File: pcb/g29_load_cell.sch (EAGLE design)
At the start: 6 parts, among them IC1 INA122P

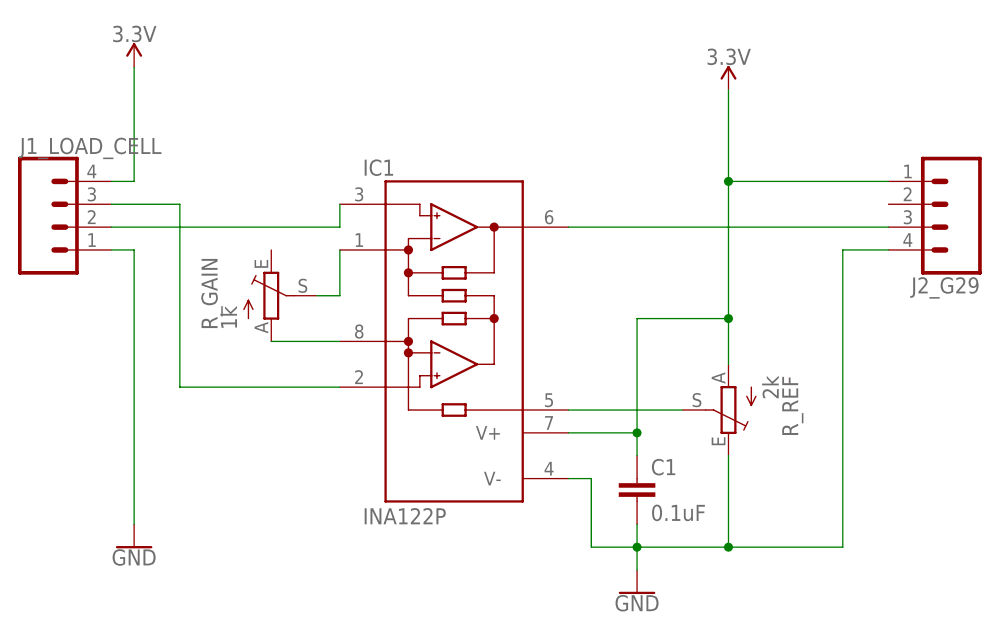
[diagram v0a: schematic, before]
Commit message: fixed ERC errors
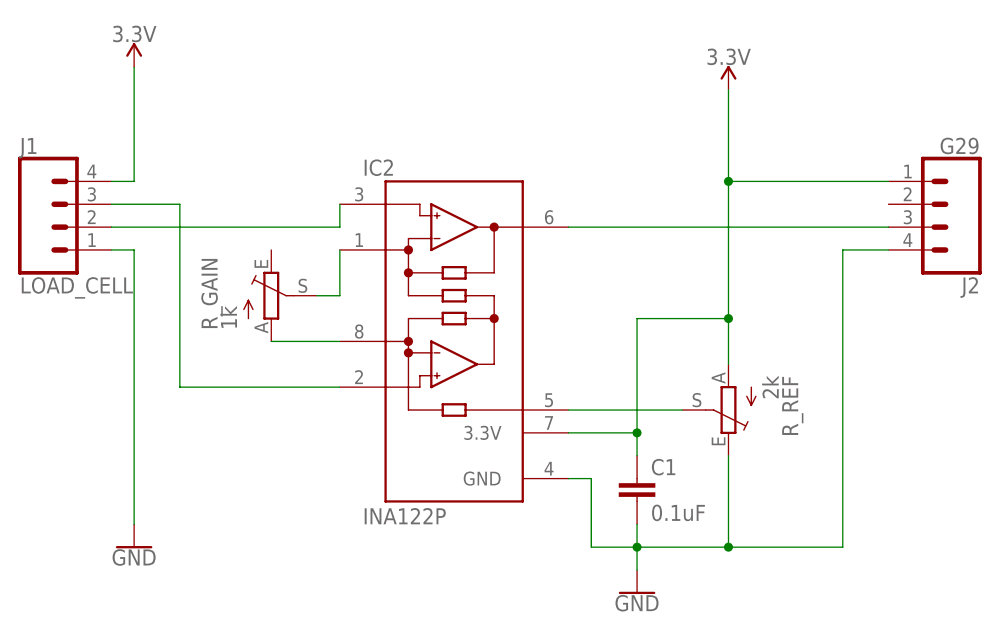
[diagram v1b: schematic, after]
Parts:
- removed IC1: INA122P, burr-brown:INA122P
- added IC2: INA122P, g29_load_cell:INA122P
- J1: value (none) -> LOAD_CELL
- J2: value (none) -> G29
- renumbered J1_LOAD_CELL to J1, J2_G29 to J2
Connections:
- net 3.3V: now also IC2.3.3V; no longer IC1.V+
- net GND: now also IC2.GND; no longer IC1.V-
- net N$1: now also IC2.RG@1; no longer IC1.RG@1
- net N$2: now also IC2.RG; no longer IC1.RG
- net N$3: now also IC2.+IN; no longer IC1.+IN
- net N$4: now also IC2.-IN; no longer IC1.-IN
- net N$6: now also IC2.REF; no longer IC1.REF
- net N$7: now also IC2.OUT; no longer IC1.OUT
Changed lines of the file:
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@@
 </classes>
 <parts>
-<part name="IC1" library="burr-brown" library_urn="urn:adsk.eagle:library:111" deviceset="INA122" device="P" package3d_urn="urn:adsk.eagle:package:4906/1"/>
 <part name="C1" library="rcl" library_urn="urn:adsk.eagle:library:334" deviceset="C-EU" device="025-024X044" package3d_urn="urn:adsk.eagle:package:23630/1" value="0.1uF"/>
 <part name="R_GAIN" library="pot" library_urn="urn:adsk.eagle:library:331" deviceset="TRIM_EU-" device="RJ9W" package3d_urn="urn:adsk.eagle:package:22702/1" value="1k"/>
 <part name="R_REF" library="pot" library_urn="urn:adsk.eagle:library:331" deviceset="TRIM_EU-" device="RJ9W" package3d_urn="urn:adsk.eagle:package:22702/1" value="2k"/>
-<part name="J1_LOAD_CELL" library="SparkFun-Connectors" deviceset="CONN_04" device="SCREW"/>
-<part name="J2_G29" library="SparkFun-Connectors" deviceset="CONN_04" device="SCREW"/>
+<part name="J1" library="SparkFun-Connectors" deviceset="CONN_04" device="SCREW" value="LOAD_CELL"/>
+<part name="J2" library="SparkFun-Connectors" deviceset="CONN_04" device="SCREW" value="G29"/>
 <part name="SUPPLY1" library="SparkFun-PowerSymbols" deviceset="3.3V" device=""/>
 <part name="GND1" library="SparkFun-PowerSymbols" deviceset="GND" device=""/>
 <part name="GND2" library="SparkFun-PowerSymbols" deviceset="GND" device=""/>
 <part name="SUPPLY2" library="SparkFun-PowerSymbols" deviceset="3.3V" device=""/>
+<part name="IC2" library="g29_load_cell" deviceset="INA122" device="P" package3d_urn="urn:adsk.eagle:package:4906/1"/>
 </parts>
 <sheets>
@@
 </plain>
 <instances>
-<instance part="IC1" gate="G$1" x="20.32" y="2.54" smashed="yes">
-<attribute name="NAME" x="10.16" y="20.955" size="1.778" layer="95" ratio="10"/>
-<attribute name="VALUE" x="10.16" y="-17.78" size="1.778" layer="96" ratio="10"/>
-</instance>
 <instance part="C1" gate="G$1" x="40.64" y="-12.7" smashed="yes">
 <attribute name="NAME" x="42.164" y="-12.319" size="1.778" layer="95"/>
@@
 <attribute name="VALUE" x="54.61" y="-1.27" size="1.778" layer="96" rot="R270"/>
 </instance>
-<instance part="J1_LOAD_CELL" gate="J1" x="-22.86" y="15.24" smashed="yes">
+<instance part="J1" gate="J1" x="-22.86" y="15.24" smashed="yes">
 <attribute name="VALUE" x="-27.94" y="7.874" size="1.778" layer="96" font="vector"/>
 <attribute name="NAME" x="-27.94" y="23.368" size="1.778" layer="95" font="vector"/>
 </instance>
-<instance part="J2_G29" gate="J1" x="73.66" y="17.78" smashed="yes" rot="R180">
+<instance part="J2" gate="J1" x="73.66" y="17.78" smashed="yes" rot="R180">
 <attribute name="VALUE" x="78.74" y="25.146" size="1.778" layer="96" font="vector" rot="R180"/>
 <attribute name="NAME" x="78.74" y="9.652" size="1.778" layer="95" font="vector" rot="R180"/>
@@
 <attribute name="VALUE" x="50.8" y="33.274" size="1.778" layer="96" align="bottom-center"/>
 </instance>
+<instance part="IC2" gate="G$1" x="20.32" y="2.54" smashed="yes">
+<attribute name="NAME" x="10.16" y="20.955" size="1.778" layer="95" ratio="10"/>
+<attribute name="VALUE" x="10.16" y="-17.78" size="1.778" layer="96" ratio="10"/>
+</instance>
 </instances>
 <busses>
@@
 <net name="N$1" class="0">
 <segment>
-<pinref part="IC1" gate="G$1" pin="RG@1"/>
 <pinref part="R_GAIN" gate="1" pin="A"/>
 <wire x1="7.62" y1="2.54" x2="0" y2="2.54" width="0.1524" layer="91"/>
+<pinref part="IC2" gate="G$1" pin="RG@1"/>
 </segment>
 </net>
 <net name="N$2" class="0">
 <segment>
-<pinref part="IC1" gate="G$1" pin="RG"/>
 <pinref part="R_GAIN" gate="1" pin="S"/>
 <wire x1="7.62" y1="12.7" x2="7.62" y2="7.62" width="0.1524" layer="91"/>
 <wire x1="7.62" y1="7.62" x2="5.08" y2="7.62" width="0.1524" layer="91"/>
+<pinref part="IC2" gate="G$1" pin="RG"/>
 </segment>
 </net>
 <net name="GND" class="0">
 <segment>
-<pinref part="J1_LOAD_CELL" gate="J1" pin="1"/>
+<pinref part="J1" gate="J1" pin="1"/>
 <wire x1="-17.78" y1="12.7" x2="-15.24" y2="12.7" width="0.1524" layer="91"/>
 <pinref part="GND1" gate="1" pin="GND"/>
@@
 </segment>
 <segment>
-<pinref part="IC1" gate="G$1" pin="V-"/>
 <wire x1="33.02" y1="-12.7" x2="35.56" y2="-12.7" width="0.1524" layer="91"/>
 <wire x1="35.56" y1="-12.7" x2="35.56" y2="-20.32" width="0.1524" layer="91"/>
@@
 <pinref part="GND2" gate="1" pin="GND"/>
 <wire x1="40.64" y1="-22.86" x2="40.64" y2="-20.32" width="0.1524" layer="91"/>
-<pinref part="J2_G29" gate="J1" pin="4"/>
+<pinref part="J2" gate="J1" pin="4"/>
 <wire x1="68.58" y1="12.7" x2="63.5" y2="12.7" width="0.1524" layer="91"/>
 <wire x1="63.5" y1="12.7" x2="63.5" y2="-20.32" width="0.1524" layer="91"/>
 <wire x1="63.5" y1="-20.32" x2="50.8" y2="-20.32" width="0.1524" layer="91"/>
 <junction x="50.8" y="-20.32"/>
+<pinref part="IC2" gate="G$1" pin="GND"/>
 </segment>
 </net>
 <net name="3.3V" class="0">
 <segment>
-<pinref part="J1_LOAD_CELL" gate="J1" pin="4"/>
+<pinref part="J1" gate="J1" pin="4"/>
 <wire x1="-17.78" y1="20.32" x2="-15.24" y2="20.32" width="0.1524" layer="91"/>
 <pinref part="SUPPLY1" gate="G$1" pin="3.3V"/>
@@
 <pinref part="R_REF" gate="1" pin="A"/>
 <wire x1="50.8" y1="30.48" x2="50.8" y2="20.32" width="0.1524" layer="91"/>
-<pinref part="J2_G29" gate="J1" pin="1"/>
+<pinref part="J2" gate="J1" pin="1"/>
 <wire x1="50.8" y1="20.32" x2="50.8" y2="5.08" width="0.1524" layer="91"/>
 <wire x1="50.8" y1="5.08" x2="50.8" y2="0" width="0.1524" layer="91"/>
 <wire x1="68.58" y1="20.32" x2="50.8" y2="20.32" width="0.1524" layer="91"/>
 <junction x="50.8" y="20.32"/>
-<pinref part="IC1" gate="G$1" pin="V+"/>
 <wire x1="33.02" y1="-7.62" x2="40.64" y2="-7.62" width="0.1524" layer="91"/>
 <pinref part="C1" gate="G$1" pin="1"/>
@@
 <junction x="40.64" y="-7.62"/>
 <junction x="50.8" y="5.08"/>
+<pinref part="IC2" gate="G$1" pin="3.3V"/>
 </segment>
 </net>
 <net name="N$6" class="0">
 <segment>
-<pinref part="IC1" gate="G$1" pin="REF"/>
 <pinref part="R_REF" gate="1" pin="S"/>
 <wire x1="33.02" y1="-5.08" x2="45.72" y2="-5.08" width="0.1524" layer="91"/>
+<pinref part="IC2" gate="G$1" pin="REF"/>
 </segment>
 </net>
 <net name="N$7" class="0">
 <segment>
-<pinref part="IC1" gate="G$1" pin="OUT"/>
-<pinref part="J2_G29" gate="J1" pin="3"/>
+<pinref part="J2" gate="J1" pin="3"/>
 <wire x1="33.02" y1="15.24" x2="68.58" y2="15.24" width="0.1524" layer="91"/>
+<pinref part="IC2" gate="G$1" pin="OUT"/>
 </segment>
 </net>
 <net name="N$3" class="0">
 <segment>
-<pinref part="J1_LOAD_CELL" gate="J1" pin="2"/>
+<pinref part="J1" gate="J1" pin="2"/>
 <wire x1="-17.78" y1="15.24" x2="7.62" y2="15.24" width="0.1524" layer="91"/>
-<pinref part="IC1" gate="G$1" pin="+IN"/>
 <wire x1="7.62" y1="15.24" x2="7.62" y2="17.78" width="0.1524" layer="91"/>
+<pinref part="IC2" gate="G$1" pin="+IN"/>
 </segment>
 </net>
 <net name="N$4" class="0">
 <segment>
-<pinref part="J1_LOAD_CELL" gate="J1" pin="3"/>
+<pinref part="J1" gate="J1" pin="3"/>
 <wire x1="-17.78" y1="17.78" x2="-10.16" y2="17.78" width="0.1524" layer="91"/>
 <wire x1="-10.16" y1="17.78" x2="-10.16" y2="-2.54" width="0.1524" layer="91"/>
-<pinref part="IC1" gate="G$1" pin="-IN"/>
 <wire x1="-10.16" y1="-2.54" x2="7.62" y2="-2.54" width="0.1524" layer="91"/>
+<pinref part="IC2" gate="G$1" pin="-IN"/>
 </segment>
 </net>
